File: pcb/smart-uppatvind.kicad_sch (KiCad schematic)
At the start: 63 parts, among them J1 PWR, J2 QWIIC, J3 UART_PROG, J4 FAN, Q1 IRLML9301, Q2 MMBT3904, Q3 MMBT3904, Q4 MMBT3904, Q5 Q_NMOS_GSD, SW1 EN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

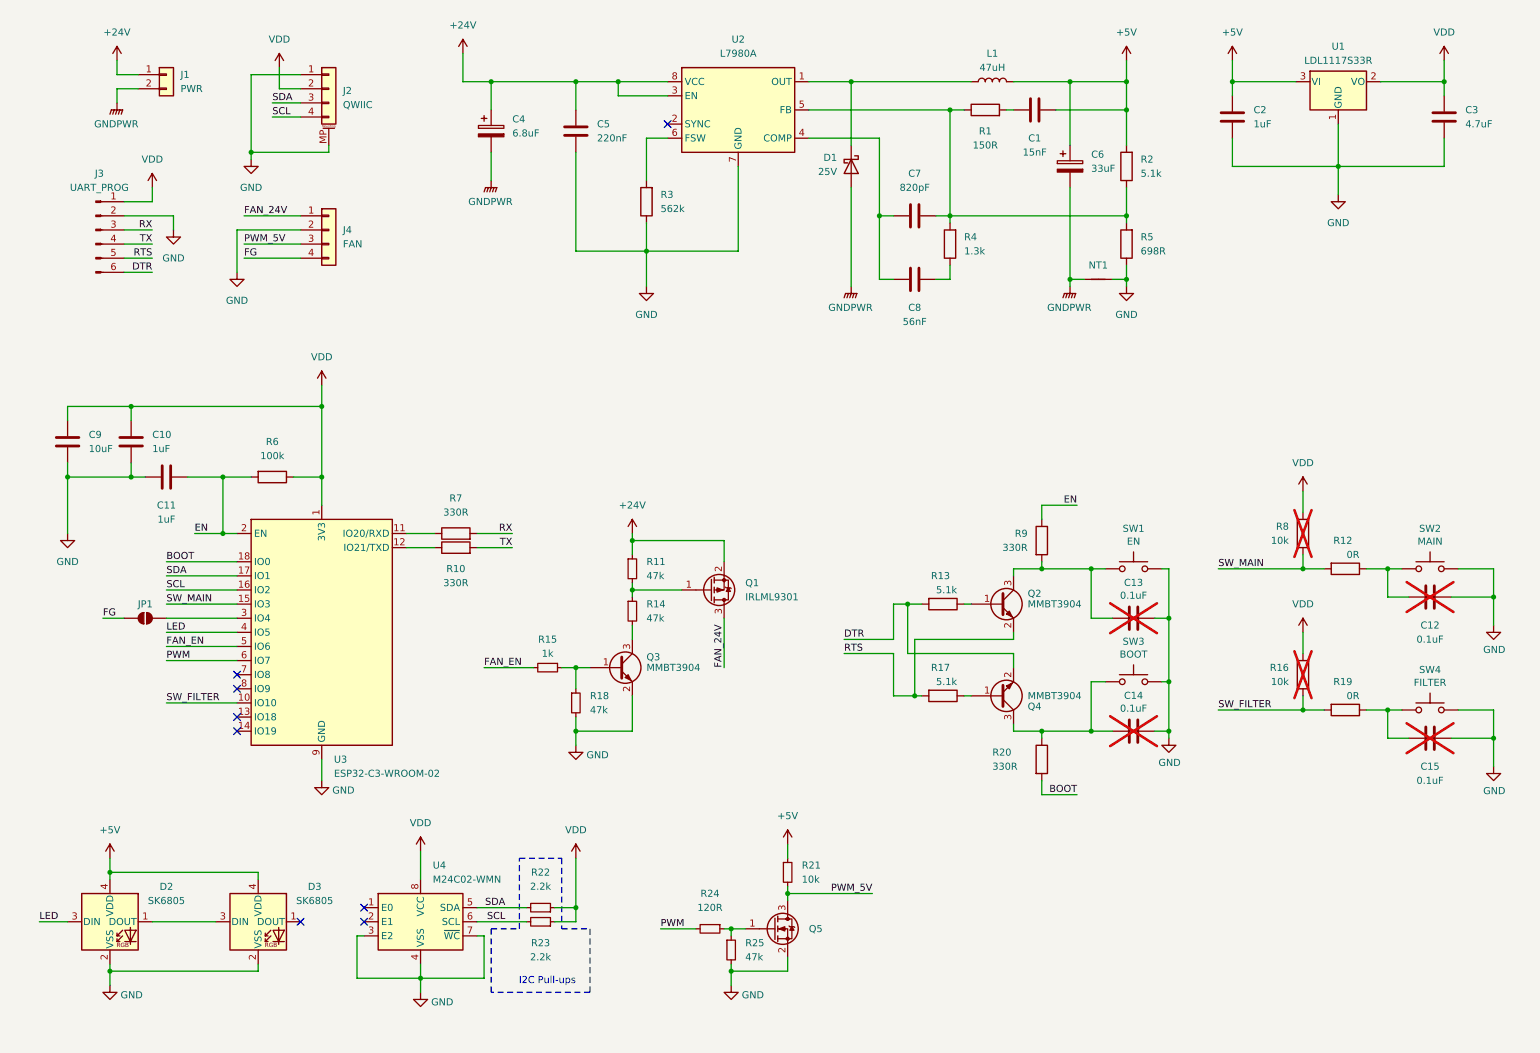
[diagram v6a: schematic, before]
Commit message: Improved the schematic readability by grouping it into named segments
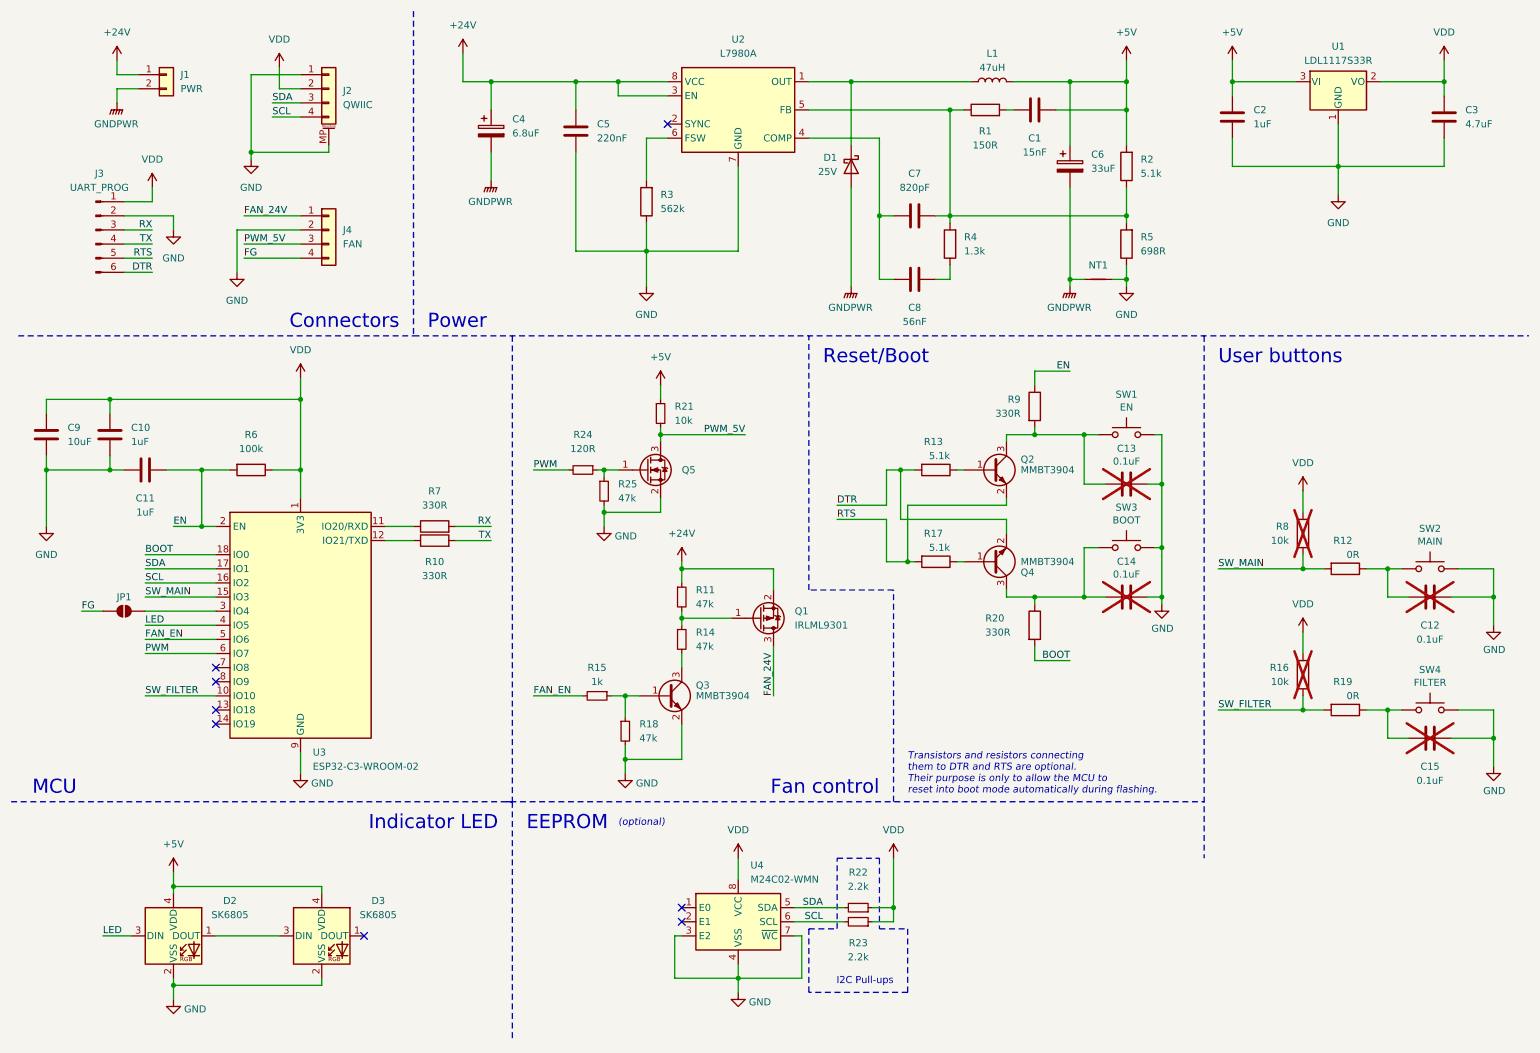
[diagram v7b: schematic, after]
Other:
- note added: "(optional)"
- note added: "Connectors"
- note added: "EEPROM"
- note added: "Fan control"
- note added: "Indicator LED"
- note added: "MCU"
- note added: "Power"
- note added: "Reset/Boot"
- note added: "Transistors and resistors connecting them to DTR and RTS are optional. Their purpose is only to allow the MCU to reset into boot mode automatically during flashing."
- note added: "User buttons"
- moved on the sheet: C10, C11, C13, C14, C9, D2, D3, JP1, Q1, Q2, Q3, Q4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

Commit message: Fixed incorrect connection of strapping pins for ESP32-C3
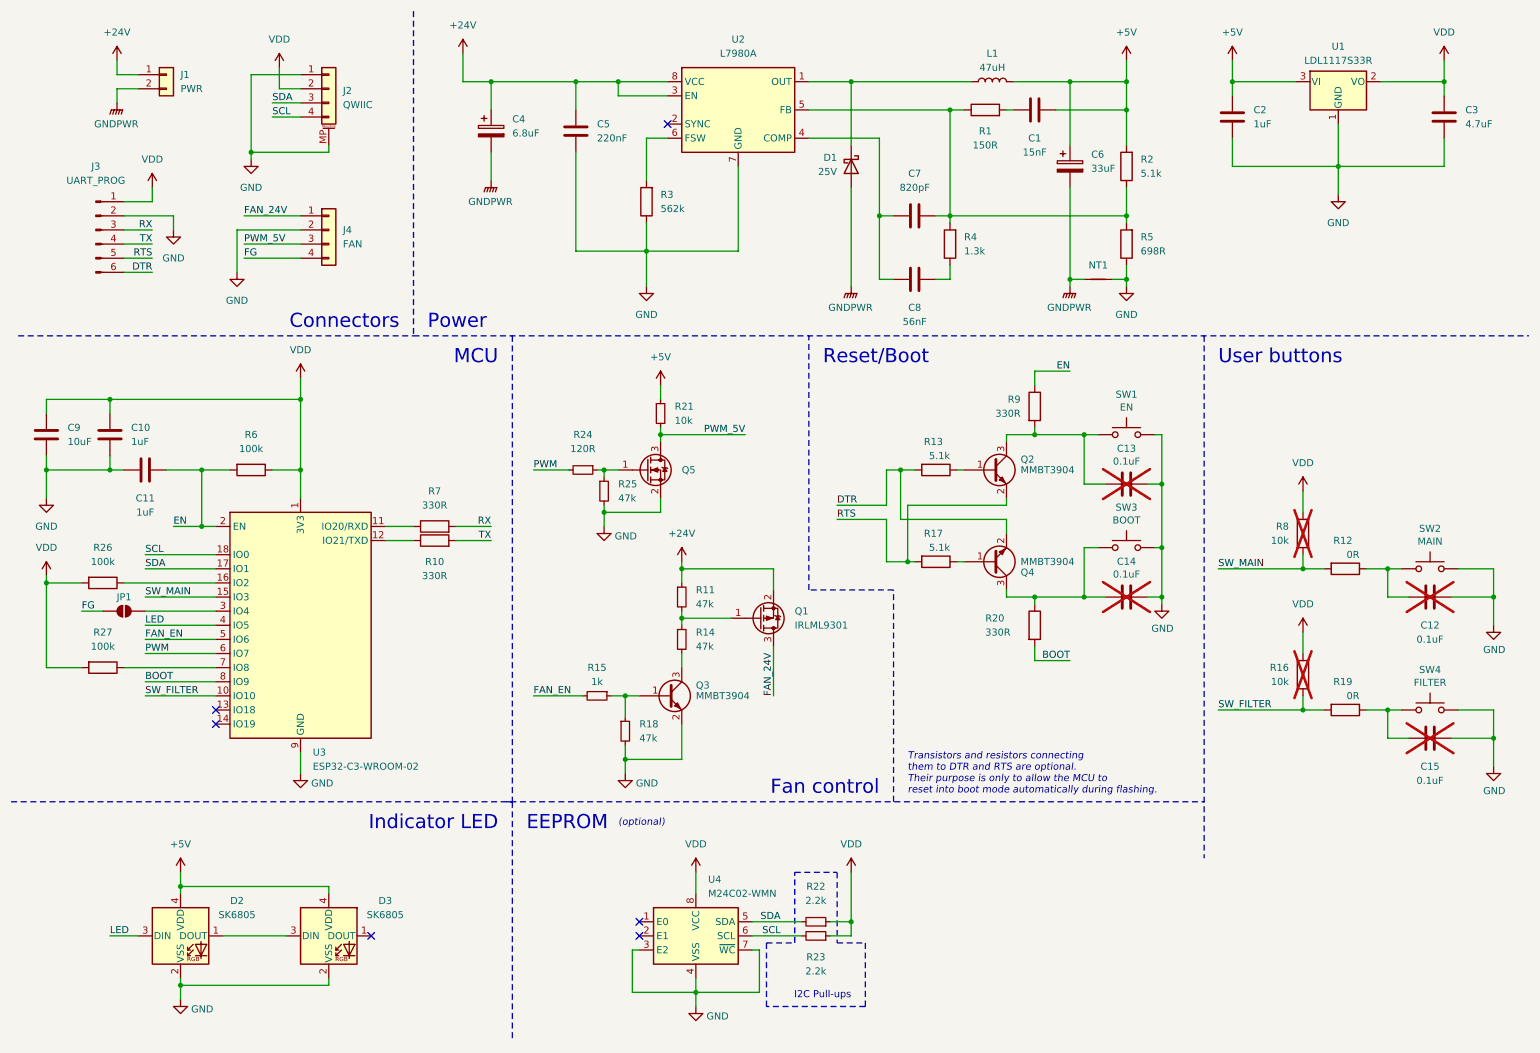
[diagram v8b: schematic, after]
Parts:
- added R26, R27: 100k, Resistor_SMD:R_0805_2012Metric, symbol Device:R
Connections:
- net BOOT: now also U3.8 (IO9); no longer U3.18 (IO0)
- net SCL: now also U3.18 (IO0); no longer U3.16 (IO2)
- net VDD: now also R26.2, R27.2
- net at U3.7 (IO8): now also R27.1
- new net: R26.1, U3.16 (IO2)
- no-connect marks 8 -> 6
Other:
- moved on the sheet: D2, D3, R22, R23, U4
